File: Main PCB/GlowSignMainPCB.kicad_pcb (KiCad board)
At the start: 2 copper layers, 140 x 71.5 mm, 130 parts, among them P1 RoundConnectorPadHole, P2 RoundConnectorPadHole, P3 RoundConnectorPadHole, P4 RoundConnectorPadHole, P5 RoundConnectorPadHole, P6 RoundConnectorPadHole, P7 RoundConnectorPadHole, P8 RoundConnectorPadHole, SW1 TS-1185EC-C-D-B, SW2 TS-1185EC-C-D-B, SW3 TS-1185EC-C-D-B, U1 AP40P05, U10 TP4056, U11 DW01A, U12 SMTSO3015CTJ, U13 SMTSO3015CTJ, U14 SMTSO3015CTJ, U15 SMTSO3015CTJ, U18 BL1117-33CX, U2 SS54, U20 GMA4030H11-F26, U26 M1250RS-02P, U3 SN74AHCT32QPWRQ1, U4 ESP32-WROOM-32E, U5 FP6298XR-G1, U6 SS54, U7 CP2102-GMR, U8 UMH3N, U9 FS8205A

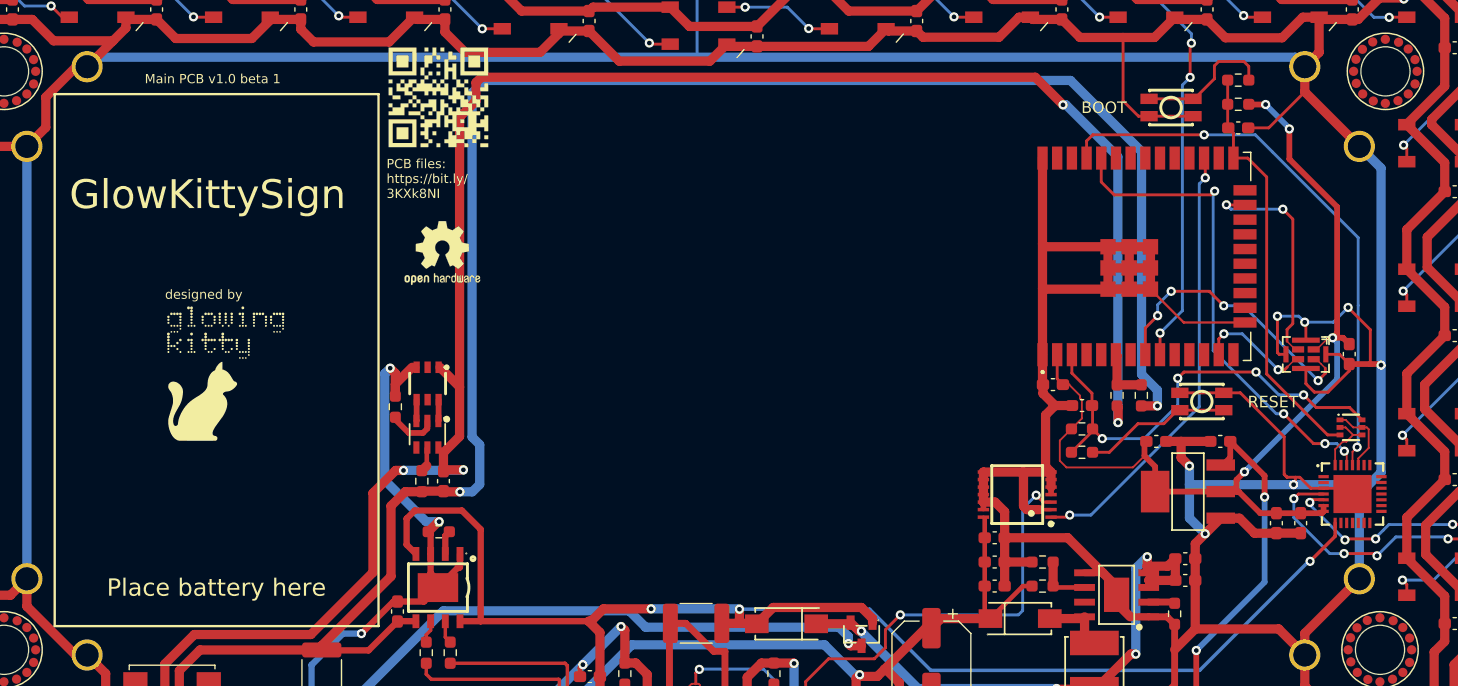
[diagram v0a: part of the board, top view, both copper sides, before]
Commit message: updated mic and levelshifter
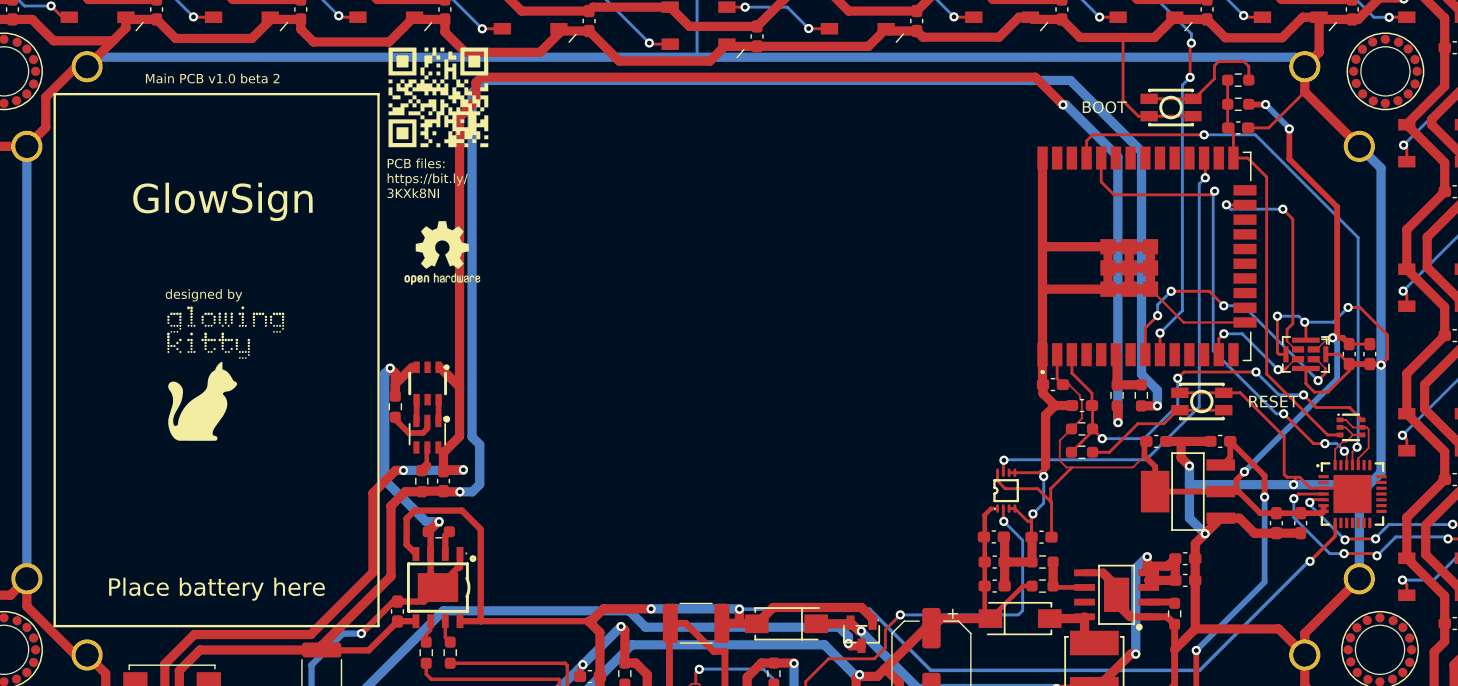
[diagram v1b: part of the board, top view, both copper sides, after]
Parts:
- added C47: 10uF, Capacitor_SMD:C_0603_1608Metric_Pad1.08x0.95mm_HandSolder, F.Cu at (209.3, 96.2)
- added C48: 0.1uF, Capacitor_SMD:C_0603_1608Metric_Pad1.08x0.95mm_HandSolder, F.Cu at (176.8, 112.1)
- C8, C9: value 1nF -> 1uF
- R16: value 73K -> 33K
- R17: value 10K -> 5.1K
- U20: value GMA4030H11-F26 -> MSM261D4030H1CPM
- U3: value SN74AHCT32QPWRQ1 -> SN74LVC2T45DCUR; footprint footprint:TSSOP-14_L5.0-W4.4-P0.65-LS6.5-BL -> footprint:VSSOP-8_L2.4-W2.1-P0.50-LS3.2-BR
- moved C2 4.05 mm to (180.9, 112.1), turned to 180 degrees
- moved U3 1.02 mm to (177.9, 108.1), turned to -90 degrees
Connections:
- C2 pad 1: +5V -> +3V3
- U3 pad 1: IO16/LED1 -> +5V
- U3 pad 2: GND -> Net-(R1-Pad1)
- U3 pad 3: Net-(R1-Pad1) -> GND
- U3 pad 7: GND -> IO16/LED1
- U3 pad 8: GND -> +3V3
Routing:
- net +3V3: track 84.9 -> 99.5 mm
- net GND: track 1063.3 -> 1050.4 mm, vias 28 -> 30
- net IO16/LED1: track 38.5 -> 41.7 mm
- net Net-(R1-Pad1): track 35.2 -> 32.7 mm
- net +5V: track 524.9 -> 526.4 mm
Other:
- board text added: "GlowSign"
- board text added: "Main PCB v1.0 beta 2"
- board text removed: "GlowKittySign"
- board text removed: "Main PCB v1.0 beta 1"

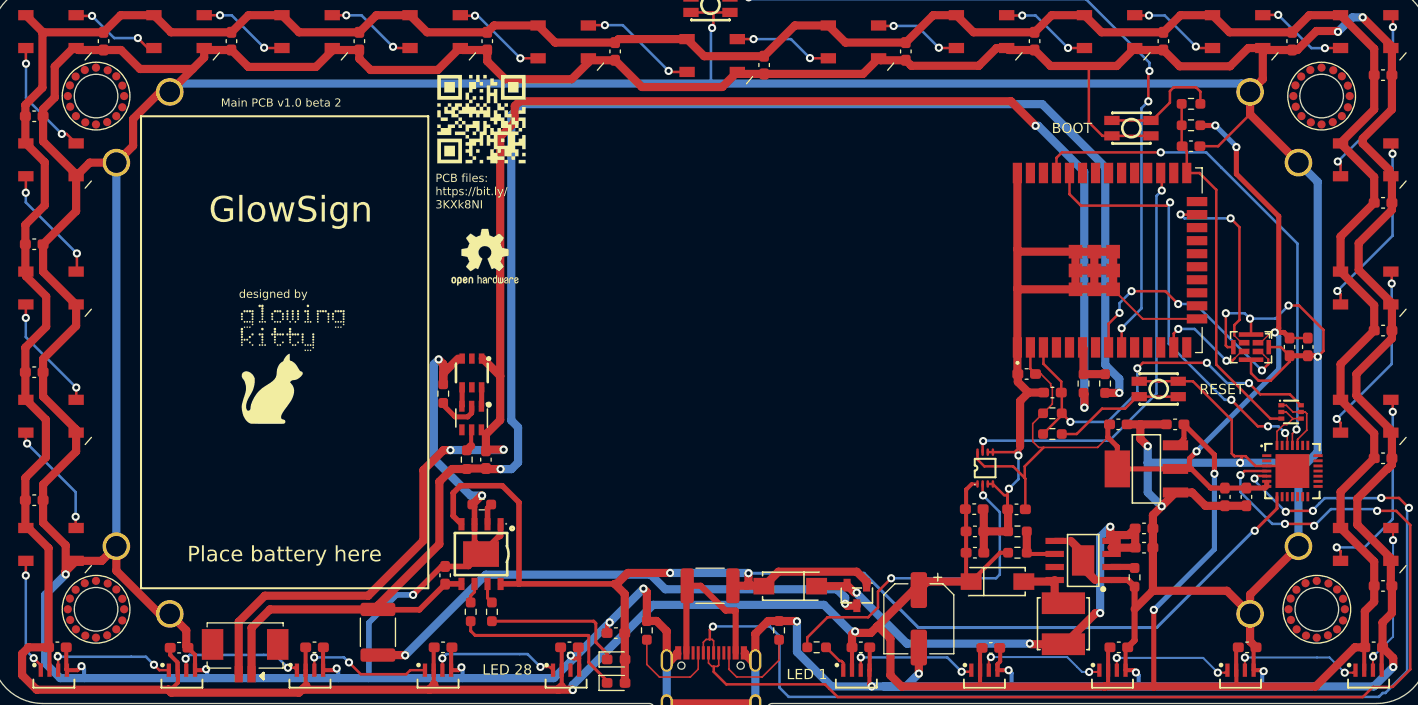
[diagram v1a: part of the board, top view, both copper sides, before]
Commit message: made improvements and started creating usb-c only version
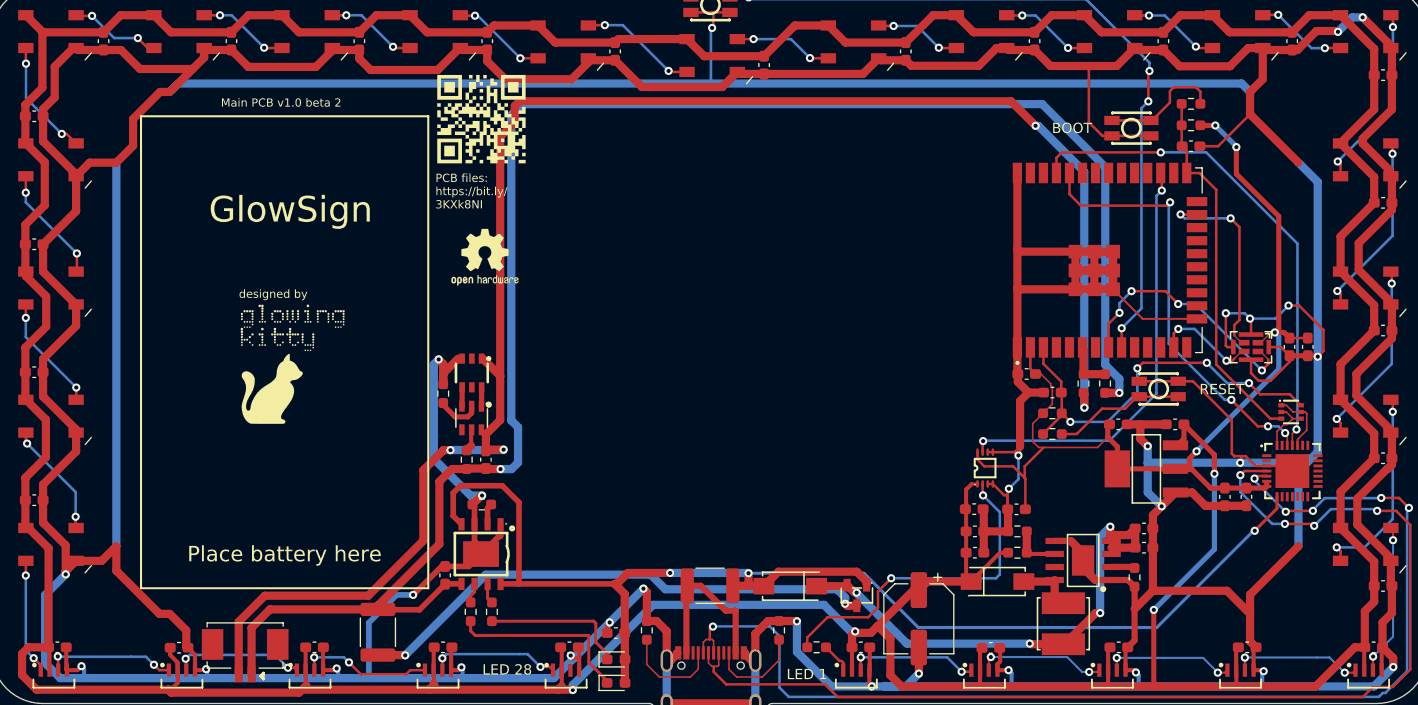
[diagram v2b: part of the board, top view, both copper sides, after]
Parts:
- removed P1, P2, P3, P4, P5, P6, P7, P8: RoundConnectorPadHole, footprint:RoundSolderPadHole
- removed U12, U13, U14, U15: SMTSO3015CTJ, footprint:SMTSO3030CTJ
- R14: value 4K -> 5.1K
- R2, R3: value 5.1K 1% -> 5.1K
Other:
- board text added: "Seamuing 2000mAh battery"

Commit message: added new glowsign design
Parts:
- removed the C18 at (165.8, 125.5)
- removed D1: green LED, LED_SMD:LED_0603_1608Metric_Pad1.05x0.95mm_HandSolder
- removed D2: red LED, LED_SMD:LED_0603_1608Metric_Pad1.05x0.95mm_HandSolder
- removed the D3 at (165.3, 128.6)
- added C22: 0.1uf, Capacitor_SMD:C_0603_1608Metric_Pad1.08x0.95mm_HandSolder, F.Cu at (233.4, 82.3)
- added C23: 0.1uf, Capacitor_SMD:C_0603_1608Metric_Pad1.08x0.95mm_HandSolder, F.Cu at (233.4, 68.7)
- added C24: 0.1uf, Capacitor_SMD:C_0603_1608Metric_Pad1.08x0.95mm_HandSolder, F.Cu at (224.7, 61.5)
- added C25: 0.1uf, Capacitor_SMD:C_0603_1608Metric_Pad1.08x0.95mm_HandSolder, F.Cu at (211.5, 61.5)
- added C41: 0.1uf, Capacitor_SMD:C_0603_1608Metric_Pad1.08x0.95mm_HandSolder, F.Cu at (69.0, 135.2)
- added C47: 0.1uf, Capacitor_SMD:C_0603_1608Metric_Pad1.08x0.95mm_HandSolder, F.Cu at (167.9, 139.6)
- added C52: 0.1uf, Capacitor_SMD:C_0603_1608Metric_Pad1.08x0.95mm_HandSolder, F.Cu at (225.5, 139.6)
- added C55: 220uF, Capacitor_SMD:C_1206_3216Metric_Pad1.33x1.80mm_HandSolder, F.Cu at (214.8, 128.3)
- added C56: 220uF, Capacitor_SMD:C_1206_3216Metric_Pad1.33x1.80mm_HandSolder, F.Cu at (211.3, 128.3)
- added D10: WS2812B, LED_SMD:LED_WS2812B_PLCC4_5.0x5.0mm_P3.2mm, F.Cu at (204.7, 62.6)
- added D26: WS2812B-4020, footprint:LED-SMD_WS2812B-4020, F.Cu at (70.3, 139.3)
- added D32: WS2812B-4020, footprint:LED-SMD_WS2812B-4020, F.Cu at (164.5, 139.3)
- added D33: WS2812B-4020, footprint:LED-SMD_WS2812B-4020, F.Cu at (178.0, 139.3)
- added D7: WS2812B, LED_SMD:LED_WS2812B_PLCC4_5.0x5.0mm_P3.2mm, F.Cu at (232.3, 76.0)
- added D8: WS2812B, LED_SMD:LED_WS2812B_PLCC4_5.0x5.0mm_P3.2mm, F.Cu at (231.4, 62.6)
- added D9: WS2812B, LED_SMD:LED_WS2812B_PLCC4_5.0x5.0mm_P3.2mm, F.Cu at (218.0, 62.6)
- added JP1: SolderJumper_2_Open, Jumper:SolderJumper-2_P1.3mm_Open_RoundedPad1.0x1.5mm, F.Cu at (204.4, 134.8)
- added JP2: SolderJumper_2_Open, Jumper:SolderJumper-2_P1.3mm_Open_RoundedPad1.0x1.5mm, F.Cu at (206.4, 134.8)
- added P1: Thermal_Pad, footprint:Thermal pad, B.Cu at (131.9, 68.1)
- added P2: Thermal_Pad, footprint:Thermal pad, B.Cu at (131.9, 135.1)
- added P3: Thermal_Pad, footprint:Thermal pad, B.Cu at (79.3, 81.6)
- added P4: Thermal_Pad, footprint:Thermal pad, B.Cu at (79.3, 113.0)
- added P5: Thermal_Pad, footprint:Thermal pad, B.Cu at (228.3, 81.6)
- added P6: Thermal_Pad, footprint:Thermal pad, B.Cu at (228.3, 113.0)
- added R18: 10K, Resistor_SMD:R_0603_1608Metric_Pad0.98x0.95mm_HandSolder, F.Cu at (218.7, 132.0)
- added R19: 10K, Resistor_SMD:R_0603_1608Metric_Pad0.98x0.95mm_HandSolder, F.Cu at (214.8, 119.7)
- added R20: 10K, Resistor_SMD:R_0603_1608Metric_Pad0.98x0.95mm_HandSolder, F.Cu at (215.3, 132.0)
- added R21: 10K, Resistor_SMD:R_0603_1608Metric_Pad0.98x0.95mm_HandSolder, F.Cu at (211.8, 132.0)
- added R22: 36K, Resistor_SMD:R_0603_1608Metric_Pad0.98x0.95mm_HandSolder, F.Cu at (175.3, 68.4)
- added R23: 5.1K, Resistor_SMD:R_0603_1608Metric_Pad0.98x0.95mm_HandSolder, F.Cu at (175.3, 70.0)
- added TP1: TestPoint, TestPoint:TestPoint_Pad_D1.5mm, F.Cu at (192.0, 134.4)
- added TP2: TestPoint, TestPoint:TestPoint_Pad_D1.5mm, F.Cu at (195.0, 134.4)
- added TP4: TestPoint, TestPoint:TestPoint_Pad_D1.5mm, F.Cu at (186.0, 134.4)
- added TP5: TestPoint, TestPoint:TestPoint_Pad_D1.5mm, F.Cu at (188.8, 134.4)
- added TP6: TestPoint, TestPoint:TestPoint_Pad_D1.5mm, F.Cu at (182.5, 134.4)
- added TP7: TestPoint, TestPoint:TestPoint_Pad_D1.5mm, F.Cu at (179.7, 134.4)
- added TP8: TestPoint, TestPoint:TestPoint_Pad_D1.5mm, F.Cu at (176.9, 134.4)
- added U12: AO3400A, footprint:SOT-23-3_L2.9-W1.6-P1.90-LS2.8-BR, F.Cu at (214.8, 122.7)
- added U13: AP40P05, footprint:SOT-23-3_L2.9-W1.3-P1.90-LS2.4-BR, F.Cu at (218.8, 134.9)
- added U14: AP40P05, footprint:SOT-23-3_L2.9-W1.3-P1.90-LS2.4-BR, F.Cu at (215.3, 134.9)
- added U15: SS54, footprint:SMA_L4.4-W2.8-LS5.4-RD, F.Cu at (186.1, 66.7)
- added U16: AP40P05, footprint:SOT-23-3_L2.9-W1.3-P1.90-LS2.4-BR, F.Cu at (211.8, 134.9)
- added U17: SS54, footprint:SMA_L4.4-W2.8-LS5.4-RD, F.Cu at (168.9, 131.9)
- C13: value 22uF -> 0.1uf
- C17: value 22uF -> 100uF; footprint Capacitor_SMD:C_0603_1608Metric_Pad1.08x0.95mm_HandSolder -> Capacitor_SMD:C_1206_3216Metric_Pad1.33x1.80mm_HandSolder
- C3: value 220uF 10V -> 220uF; footprint Capacitor_SMD:CP_Elec_6.3x5.4 -> Capacitor_SMD:C_1206_3216Metric_Pad1.33x1.80mm_HandSolder
- R10, R11: value 1K -> 100K
- R12, R16: value 33K -> 100K
- R17: value 5.1K -> 62K
- SW3: value TS-1185EC-C-D-B -> TS24CA; footprint footprint:SW-SMD_4P-L3.7-W3.0-P1.50-LS4.7 -> footprint:SW-SMD_TS24CA
- U1: value AP40P05 -> S8050; footprint footprint:SOT-23-3_L2.9-W1.3-P1.90-LS2.4-BR -> footprint:SOT-23-3_L3.0-W1.7-P0.95-LS2.9-BR
- U5: value FP6298XR-G1 -> FP6276BXR-G1
- moved C14 93.9 mm to (204.1, 67.6), turned to 0 degrees
- moved R14 91.6 mm to (211.0, 71.2), turned to 90 degrees
- moved U10 89.7 mm to (206.2, 71.1), turned to 90 degrees
- moved C11 79.4 mm to (204.1, 74.8), turned to 180 degrees
- moved R15 79.4 mm to (196.2, 67.6)
- moved C15 79.3 mm to (197.9, 67.6)
- moved U11 78.4 mm to (200.4, 73.6)
- moved U9 78.4 mm to (200.5, 69.2)
- moved R13 78.3 mm to (197.9, 72.0)
- moved SW3 77.2 mm to (158.3, 139.8)
- moved U26 69.7 mm to (144.5, 69.0)
- moved F2 67.2 mm to (154.7, 67.4), turned to 0 degrees
- moved R1 66.0 mm to (227.4, 122.5)
- moved L1 60.2 mm to (161.1, 68.2), turned to 180 degrees
- moved C12 58.9 mm to (156.2, 70.1), turned to 180 degrees
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- renumbered C23 to C18, C24 to C19, C25 to C20, C26 to C21, C27 to C26, C28 to C27, C29 to C28, C30 to C29, C31 to C30, C32 to C31, C33 to C32, C34 to C33, C35 to C34, C36 to C35, C37 to C36, C38 to C37, C39 to C38, C40 to C39, C41 to C40, C19 to C48, C20 to C49, C21 to C50, C22 to C51, C47 to C53, C48 to C54, D12 to D11, D13 to D12, D14 to D13, D15 to D14, D16 to D15, D17 to D16, D18 to D17, D19 to D18, D20 to D19, D21 to D20, D22 to D21, D23 to D22, D24 to D23, D25 to D24, D26 to D25, D8 to D3, D4 to D34, D5 to D35, D6 to D36, D7 to D37, D9 to D4, D10 to D5, D11 to D6
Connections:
- net RESET renamed EN
- C11 pad 2: USB-C 5V -> VBUS
- C13 pad 1: Net-(C12-Pad1) -> Net-(C13-Pad1)
- C16 pad 1: +5V -> Net-(C16-Pad1)
- C17 pad 1: +5V -> Net-(C16-Pad1)
- C18 pad 1: +5V -> LED 5V
- C19 pad 1: +5V -> LED 5V
- C20 pad 1: +5V -> LED 5V
- C21 pad 1: +5V -> LED 5V
- C26 pad 1: +5V -> LED 5V
- C27 pad 1: +5V -> LED 5V
- C28 pad 1: +5V -> LED 5V
- C29 pad 1: +5V -> LED 5V
- C30 pad 1: +5V -> LED 5V
- C31 pad 1: +5V -> LED 5V
- C32 pad 1: +5V -> LED 5V
- C33 pad 1: +5V -> LED 5V
- C34 pad 1: +5V -> LED 5V
- C35 pad 1: +5V -> LED 5V
- C36 pad 1: +5V -> LED 5V
- C37 pad 1: +5V -> LED 5V
- C38 pad 1: +5V -> LED 5V
- C39 pad 1: +5V -> LED 5V
- C40 pad 1: +5V -> LED 5V
- C42 pad 1: +5V -> LED 5V
- C43 pad 1: +5V -> LED 5V
- C44 pad 1: +5V -> LED 5V
- C45 pad 1: +5V -> LED 5V
- C46 pad 1: +5V -> LED 5V
- C48 pad 1: +5V -> LED 5V
- C49 pad 1: +5V -> LED 5V
- C50 pad 1: +5V -> LED 5V
- C51 pad 1: +5V -> LED 5V
- D11 pad 1: +5V -> LED 5V
- D11 pad 4: Net-(D11-Pad2) (its old number) -> Net-(D10-Pad2)
- D12 pad 1: +5V -> LED 5V
- D13 pad 1: +5V -> LED 5V
- D14 pad 1: +5V -> LED 5V
- D15 pad 1: +5V -> LED 5V
- D16 pad 1: +5V -> LED 5V
- D17 pad 1: +5V -> LED 5V
- D18 pad 1: +5V -> LED 5V
- D19 pad 1: +5V -> LED 5V
- D20 pad 1: +5V -> LED 5V
- D21 pad 1: +5V -> LED 5V
- D22 pad 1: +5V -> LED 5V
- D23 pad 1: +5V -> LED 5V
- D24 pad 1: +5V -> LED 5V
- D25 pad 1: +5V -> LED 5V
- D25 pad 2: Net-(D26-Pad2) -> Net-(D25-Pad2)
- D27 pad 1: Net-(D26-Pad2) -> Net-(D26-Pad3)
- D27 pad 2: +5V -> LED 5V
- D28 pad 2: +5V -> LED 5V
- D29 pad 2: +5V -> LED 5V
- D3 pad 1: +5V -> LED 5V
- D3 pad 4: Net-(D7-Pad3) -> LED1 DATA OUT
- D30 pad 2: +5V -> LED 5V
- D31 pad 2: +5V -> LED 5V
- D31 pad 3: unconnected-(D31-Pad3) -> Net-(D31-Pad3)
- D34 pad 2: +5V -> LED 5V
- D35 pad 2: +5V -> LED 5V
- D36 pad 2: +5V -> LED 5V
- D37 pad 2: +5V -> LED 5V
- D37 pad 3: Net-(D7-Pad3) -> unconnected-(D37-Pad3)
- D4 pad 1: +5V -> LED 5V
- D5 pad 1: +5V -> LED 5V
- D6 pad 1: +5V -> LED 5V
- D6 pad 2: Net-(D11-Pad2) (its old number) -> Net-(D6-Pad2)
- F1 pad 2: USB-C 5V -> Net-(F1-Pad2)
- F2 pad 2: Net-(F2-Pad2) -> Net-(C12-Pad1)
- R10 pad 1: Net-(R10-Pad1) -> IO25/VBUS
- R10 pad 2: Net-(D1-Pad1) -> VBUS
- R11 pad 1: Net-(R11-Pad1) -> GND
- R11 pad 2: Net-(D2-Pad1) -> IO25/VBUS
- R12 pad 1: GND -> VBUS
- R16 pad 1: +5V -> Net-(C12-Pad1)
- R16 pad 2: Net-(R16-Pad2) -> Net-(C13-Pad1)
- R17 pad 1: Net-(R16-Pad2) -> Net-(R17-Pad1)
- R8 pad 1: I34/BATTVOLT -> IO26/BATT VOLT
- R9 pad 2: I34/BATTVOLT -> IO26/BATT VOLT
- SW3 pad 1: GND -> unconnected-(SW3-Pad1)
- SW3 pad 2: IO33/MAINBUTTON -> unconnected-(SW3-Pad2)
- U1 pad 1: USB-C 5V -> Net-(R12-Pad2)
- U1 pad 2: Net-(C12-Pad1) -> GND
- U1 pad 3: Net-(F2-Pad2) -> Net-(C13-Pad1)
- U10 pad 4: USB-C 5V -> VBUS
- U10 pad 6: Net-(R10-Pad1) -> unconnected-(U10-Pad6)
- U10 pad 7: Net-(R11-Pad1) -> IO27/BATT CHARGING
- U10 pad 8: USB-C 5V -> VBUS
- U2 pad 1: Net-(C12-Pad1) -> +5V
- U2 pad 2: USB-C 5V -> Net-(F1-Pad2)
- U4 pad 10: unconnected-(U4-Pad10) -> IO25/VBUS
- U4 pad 11: unconnected-(U4-Pad11) -> IO26/BATT VOLT
- U4 pad 12: unconnected-(U4-Pad12) -> IO27/BATT CHARGING
- U4 pad 30: unconnected-(U4-Pad30) -> IO18/MAINBUTTON
- U4 pad 31: unconnected-(U4-Pad31) -> IO19
- U4 pad 37: unconnected-(U4-Pad37) -> IO23/LEDPOWER
- U4 pad 6: I34/BATTVOLT -> unconnected-(U4-Pad6)
- U4 pad 9: IO33/MAINBUTTON -> unconnected-(U4-Pad9)
- U5 pad 1: GND -> Net-(L1-Pad2)
- U5 pad 2: Net-(R12-Pad2) -> Net-(L1-Pad2)
- U5 pad 4: Net-(C12-Pad1) -> Net-(C13-Pad1)
- U5 pad 6: Net-(R16-Pad2) -> Net-(R22-Pad1)
- U5 pad 7: unconnected-(U5-Pad7) -> Net-(R17-Pad1)
- U5 pad 8: Net-(L1-Pad2) -> Net-(C16-Pad1)
- U6 pad 2: Net-(L1-Pad2) -> Net-(C16-Pad1)
- U7 pad 8: USB-C 5V -> VBUS
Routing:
- net LED 5V: track 0.00 -> 650.1 mm, vias 0 -> 72
- net +5V: track 526.4 -> 173.9 mm, vias 4 -> 0
- net VBUS: track 0.00 -> 180.0 mm, vias 0 -> 5
- net USB-C 5V: track 128.8 -> 0.00 mm, vias 3 -> 0
- net IO18/MAINBUTTON: track 0.00 -> 101.6 mm, vias 0 -> 7
- net IO26/BATT VOLT: track 0.00 -> 95.7 mm, vias 0 -> 3
- net IO33/MAINBUTTON: track 76.2 -> 0.00 mm, vias 4 -> 0
- net IO25/VBUS: track 0.00 -> 65.8 mm
- net IO23/LEDPOWER: track 0.00 -> 51.9 mm, vias 0 -> 2
- net Net-(F2-Pad2): track 51.6 -> 0.00 mm, vias 2 -> 0
- net GND: track 1050.4 -> 1002.7 mm, vias 30 -> 129
- net IO27/BATT CHARGING: track 0.00 -> 44.2 mm, vias 0 -> 2
- net +3V3: track 99.5 -> 138.8 mm, vias 4 -> 12
- net IO15/WS: track 19.9 -> 53.4 mm, vias 2 -> 6
- net IO16/LED1: track 41.7 -> 75.1 mm, vias 2 -> 6
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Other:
- board size 140 x 71.5 mm -> 169.5 x 83.5 mm
- board text added: "3.3V"
- board text added: "5V"
- board text added: "B+"
- board text added: "B-"
- board text added: "G"
- board text added: "L1"
- board text added: "LED 0"
- board text added: "MB"
- board text added: "Seamuing 3000mAh battery"
- board text removed: "LED 1"
- board text removed: "LED 28"
- board text removed: "Place battery here"
- board text removed: "Seamuing 2000mAh battery"
